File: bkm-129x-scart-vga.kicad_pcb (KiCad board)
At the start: 2 copper layers, 105 x 160 mm, 69 parts, among them J1 DB15_Female_HighDensity_Mount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, J2 SCART-F, J3 SJ1-353XNG, J4 UART, J5 Conn_02x32_Row_Letter_Last, J6 ICSP, Q1 DTC144EKA, Q2 MMBT3904, SW1 PBH4UEENAGX, SW2 PBH4UEENAGX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

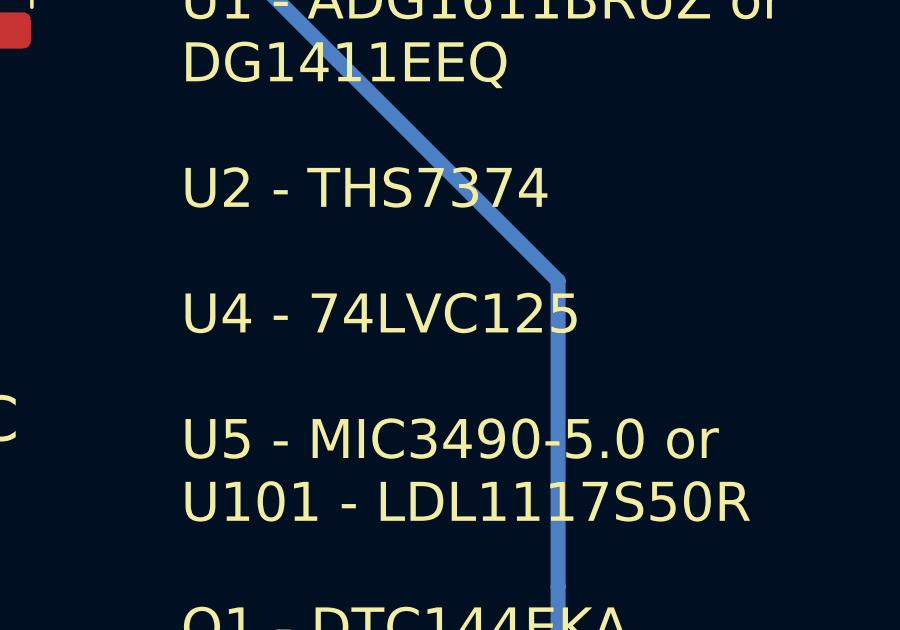
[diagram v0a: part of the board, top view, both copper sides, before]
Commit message: Edit PCB silkscreen BOM description: 74VHC125 not 74LVC125 See comment https://www.reddit.com/r/crtgaming/comments/f5u1zo/bkm129x_cheapedition/ 74LVC125AD112 (NXP/Nexperia) is not compatible. Tested and confirmed working with MC74VHCT125ADR2G (ON Semiconductor).
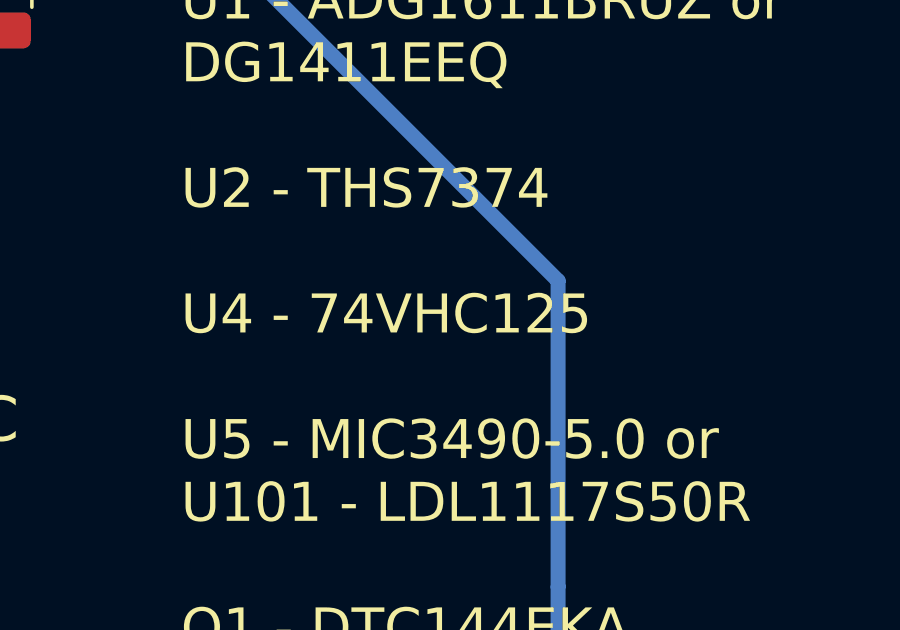
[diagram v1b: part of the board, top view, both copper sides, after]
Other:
- board text added: "U1 - ADG1611BRUZ or DG1411EEQ U2 - THS7374 U4 - 74VHC125 U5 - MIC3490-5.0 or U101 - LDL1117S50R Q1 - DTC144EKA Q2 - MMBT3904 D1 - RED 0805 LED D2 - GREEN 0805 LED U1/2/4: TSSOP14 SW1/SW2: SPUJ193700 J3: CUI SJ1-353XNG (Like SJ1-3533NG)"
- board text removed: "U1 - ADG1611BRUZ or DG1411EEQ U2 - THS7374 U4 - 74LVC125 U5 - MIC3490-5.0 or U101 - LDL1117S50R Q1 - DTC144EKA Q2 - MMBT3904 D1 - RED 0805 LED D2 - GREEN 0805 LED U1/2/4: TSSOP14 SW1/SW2: SPUJ193700 J3: CUI SJ1-353XNG (Like SJ1-3533NG)"
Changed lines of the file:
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@@
 		)
 	)
-	(gr_text "U1 - ADG1611BRUZ or\nDG1411EEQ\n\nU2 - THS7374\n\nU4 - 74LVC125\n\nU5 - MIC3490-5.0 or\nU101 - LDL1117S50R\n\nQ1 - DTC144EKA\nQ2 - MMBT3904\nD1 - RED 0805 LED\nD2 - GREEN 0805 LED\nU1/2/4: TSSOP14\nSW1/SW2: SPUJ193700\nJ3: CUI SJ1-353XNG\n(Like SJ1-3533NG)"
+	(gr_text "U1 - ADG1611BRUZ or\nDG1411EEQ\n\nU2 - THS7374\n\nU4 - 74VHC125\n\nU5 - MIC3490-5.0 or\nU101 - LDL1117S50R\n\nQ1 - DTC144EKA\nQ2 - MMBT3904\nD1 - RED 0805 LED\nD2 - GREEN 0805 LED\nU1/2/4: TSSOP14\nSW1/SW2: SPUJ193700\nJ3: CUI SJ1-353XNG\n(Like SJ1-3533NG)"
 		(at 84.0105 50.673 0)
 		(layer "F.SilkS")
